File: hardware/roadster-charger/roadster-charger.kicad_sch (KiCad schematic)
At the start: 62 parts, among them J1 USB4505-03-0-A, J2 USB4505-03-0-A, J3 54-00166, Q1 CSD19532Q5B, U1 FUSB307BMPX, U10 OPA340NA, U11 LM75B, U2 ESP32-C3-MINI-1, U3 INA168, U4 LM5050-1, U5 INA168, U6 OPA340NA, U9 MPM3606AGQV-P

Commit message: add in some missing PNs
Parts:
- H1, H2: MPN (none) -> DNP; now left out of the parts list
- TP1, TP2, TP3, TP4: MPN (none) -> RCU-0C
- U11: MPN (none) -> LM75BDP
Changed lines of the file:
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@@
 (kicad_sch (version 20230121) (generator eeschema)
   (paper "B")
+  (title_block
+    (rev "1")
+  )
   (junction (at 133.35 78.74) (diameter 0) (color 0 0 0 0)
   )
@@
   )
   (symbol (lib_id "Mechanical:MountingHole") (at 400.05 238.76 0) (unit 1)
-    (in_bom yes) (on_board yes) (dnp no) (fields_autoplaced)
+    (in_bom no) (on_board yes) (dnp no) (fields_autoplaced)
     (property "Reference" "H1" (at 402.59 237.49 0)
       (effects (font (size 1.27 1.27)) (justify left))
@@
       (effects (font (size 1.27 1.27)) hide)
     )
+    (property "MPN" "DNP" (at 400.05 238.76 0)
+      (effects (font (size 1.27 1.27)) hide)
+    )
     (instances
       (project "roadster-charger"
@@
   )
   (symbol (lib_id "Mechanical:MountingHole") (at 400.05 245.11 0) (unit 1)
-    (in_bom yes) (on_board yes) (dnp no) (fields_autoplaced)
+    (in_bom no) (on_board yes) (dnp no) (fields_autoplaced)
     (property "Reference" "H2" (at 402.59 243.84 0)
       (effects (font (size 1.27 1.27)) (justify left))
@@
       (effects (font (size 1.27 1.27)) hide)
     )
+    (property "MPN" "DNP" (at 400.05 245.11 0)
+      (effects (font (size 1.27 1.27)) hide)
+    )
     (instances
       (project "roadster-charger"
@@
       (effects (font (size 1.27 1.27)) hide)
     )
+    (property "MPN" "LM75BDP" (at 189.23 180.34 0)
+      (effects (font (size 1.27 1.27)) hide)
+    )
     (pin "6")
     (pin "8")
@@
       (effects (font (size 1.27 1.27)) hide)
     )
+    (property "MPN" "RCU-0C" (at 201.93 31.75 0)
+      (effects (font (size 1.27 1.27)) hide)
+    )
     (pin "1")
     (instances
@@
       (effects (font (size 1.27 1.27)) hide)
     )
+    (property "MPN" "RCU-0C" (at 119.38 219.71 0)
+      (effects (font (size 1.27 1.27)) hide)
+    )
     (pin "1")
     (instances
@@
       (effects (font (size 1.27 1.27)) hide)
     )
+    (property "MPN" "RCU-0C" (at 191.77 31.75 0)
+      (effects (font (size 1.27 1.27)) hide)
+    )
     (pin "1")
     (instances
@@
       (effects (font (size 1.27 1.27)) hide)
     )
+    (property "MPN" "RCU-0C" (at 196.85 31.75 0)
+      (effects (font (size 1.27 1.27)) hide)
+    )

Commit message: run schematic annotation to clean up error
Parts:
- removed H1, H2: MountingHole, MountingHole:MountingHole_3.2mm_M3_ISO7380_Pad_TopBottom, symbol Mechanical:MountingHole
- added H1, H2: MountingHole_Pad, MountingHole:MountingHole_3.2mm_M3_ISO7380_Pad_TopBottom, symbol Mechanical:MountingHole_Pad
- renumbered C4 to C10, C5 to C11, C22 to C12, C8 to C13, C9 to C14, C21 to C15, C6 to C16, C10 to C3, C3 to C4, C18 to C5, C11 to C6, C20 to C7, C27 to C8, C19 to C9, D5 to D4, D4 to D5, D7 to D6, R5 to R1, R2 to R10, R3 to R11, R4 to R12, R9 to R13, R12 to R14, R13 to R15, R8 to R16, R6 to R17, R10 to R18, R11 to R19, R19 to R2, R23 to R20, R24 to R21, R21 to R3, R26 to R4, R20 to R5, R25 to R6, R22 to R7, R7 to R8, R1 to R9, TP4 to TP1, TP1 to TP2, TP2 to TP3, TP3 to TP4, U9 to U1, U10 to U4, U1 to U5, U11 to U6, U4 to U7, U5 to U8, U6 to U9
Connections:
- net GND: now also H1.1, H2.1

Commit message: clean up fab layer, add value to test points
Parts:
- TP1, TP2, TP3, TP4: value TestPoint -> RCU-0C
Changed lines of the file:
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@@
       (effects (font (size 1.27 1.27)) (justify left))
     )
-    (property "Value" "TestPoint" (at 204.47 29.718 0)
+    (property "Value" "RCU-0C" (at 204.47 29.718 0)
       (effects (font (size 1.27 1.27)) (justify left) hide)
     )
@@
       (effects (font (size 1.27 1.27)) (justify left))
     )
-    (property "Value" "TestPoint" (at 116.84 221.742 0)
+    (property "Value" "RCU-0C" (at 116.84 221.742 0)
       (effects (font (size 1.27 1.27)) (justify left) hide)
     )
@@
       (effects (font (size 1.27 1.27)) (justify left))
     )
-    (property "Value" "TestPoint" (at 194.31 29.718 0)
+    (property "Value" "RCU-0C" (at 194.31 29.718 0)
       (effects (font (size 1.27 1.27)) (justify left) hide)
     )
@@
       (effects (font (size 1.27 1.27)) (justify left))
     )
-    (property "Value" "TestPoint" (at 199.39 29.718 0)
+    (property "Value" "RCU-0C" (at 199.39 29.718 0)
       (effects (font (size 1.27 1.27)) (justify left) hide)
     )

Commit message: add IO9 test point for when I accidentally reassign usb pins during fw dev
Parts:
- added TP1: RCU-0C, RCU-0C:TP+195X110, symbol Connector:TestPoint
- renumbered TP1 to TP2, TP2 to TP3, TP3 to TP4, TP4 to TP5
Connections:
- net IO9_BOOT: now reaches U2.23 (GPIO9)
- net IO9_BOOT: now also TP1.1
- no-connect marks 25 -> 24
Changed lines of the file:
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@@
   (no_connect (at 58.42 57.15))
   (no_connect (at 179.07 182.88))
-  (no_connect (at 96.52 234.95))
   (no_connect (at 179.07 43.18))
   (no_connect (at 179.07 53.34))
@@
     (stroke (width 0) (type default))
   )
+  (wire (pts (xy 96.52 234.95) (xy 111.76 234.95))
+    (stroke (width 0) (type default))
+  )
   (wire (pts (xy 287.02 161.29) (xy 292.1 161.29))
     (stroke (width 0) (type default))
@@
     (effects (font (size 1.27 1.27)) (justify right bottom))
   )
+  (label "IO9_BOOT" (at 109.22 234.95 180) (fields_autoplaced)
+    (effects (font (size 1.27 1.27)) (justify right bottom))
+  )
   (label "V_SW" (at 71.12 138.43 0) (fields_autoplaced)
     (effects (font (size 1.27 1.27)) (justify left bottom))
@@
     )
   )
+  (symbol (lib_id "Connector:TestPoint") (at 111.76 234.95 270) (unit 1)
+    (in_bom yes) (on_board yes) (dnp no)
+    (property "Reference" "TP1" (at 113.03 232.41 90)
+      (effects (font (size 1.27 1.27)) (justify left))
+    )
+    (property "Value" "RCU-0C" (at 113.792 237.49 0)
+      (effects (font (size 1.27 1.27)) (justify left) hide)
+    )
+    (property "Footprint" "RCU-0C:TP+195X110" (at 111.76 240.03 0)
+      (effects (font (size 1.27 1.27)) hide)
+    )
+    (property "Datasheet" "~" (at 111.76 240.03 0)
+      (effects (font (size 1.27 1.27)) hide)
+    )
+    (property "MPN" "RCU-0C" (at 111.76 234.95 0)
+      (effects (font (size 1.27 1.27)) hide)
+    )
+    (pin "1")
+    (instances
+      (project "roadster-charger"
+        (path "/57ecac41-cd8a-4182-a81e-fed3e381aedd"
+          (reference "TP1") (unit 1)
+        )
+      )
+    )
+  )
   (symbol (lib_id "Device:R_Small") (at 222.25 29.21 0) (unit 1)
     (in_bom yes) (on_board yes) (dnp no)
@@
   (symbol (lib_id "Connector:TestPoint") (at 201.93 31.75 0) (unit 1)
     (in_bom yes) (on_board yes) (dnp no)
-    (property "Reference" "TP4" (at 200.025 26.035 0)
+    (property "Reference" "TP5" (at 200.025 26.035 0)
       (effects (font (size 1.27 1.27)) (justify left))
     )
@@
       (project "roadster-charger"
         (path "/57ecac41-cd8a-4182-a81e-fed3e381aedd"
-          (reference "TP4") (unit 1)
+          (reference "TP5") (unit 1)
         )
       )
@@
   (symbol (lib_id "Connector:TestPoint") (at 119.38 219.71 180) (unit 1)
     (in_bom yes) (on_board yes) (dnp no)
-    (property "Reference" "TP1" (at 121.285 225.425 0)
+    (property "Reference" "TP2" (at 121.285 225.425 0)
       (effects (font (size 1.27 1.27)) (justify left))
     )
@@
       (project "roadster-charger"
         (path "/57ecac41-cd8a-4182-a81e-fed3e381aedd"
-          (reference "TP1") (unit 1)
+          (reference "TP2") (unit 1)
         )
       )
@@
   (symbol (lib_id "Connector:TestPoint") (at 191.77 31.75 0) (unit 1)
     (in_bom yes) (on_board yes) (dnp no)
-    (property "Reference" "TP2" (at 189.865 26.035 0)
+    (property "Reference" "TP3" (at 189.865 26.035 0)
       (effects (font (size 1.27 1.27)) (justify left))
     )
@@
       (project "roadster-charger"
         (path "/57ecac41-cd8a-4182-a81e-fed3e381aedd"
-          (reference "TP2") (unit 1)
+          (reference "TP3") (unit 1)
         )
       )
@@
   (symbol (lib_id "Connector:TestPoint") (at 196.85 31.75 0) (unit 1)
     (in_bom yes) (on_board yes) (dnp no)
-    (property "Reference" "TP3" (at 194.945 26.035 0)
+    (property "Reference" "TP4" (at 194.945 26.035 0)
       (effects (font (size 1.27 1.27)) (justify left))
     )
@@
       (project "roadster-charger"
         (path "/57ecac41-cd8a-4182-a81e-fed3e381aedd"
-          (reference "TP3") (unit 1)
+          (reference "TP4") (unit 1)
         )
       )

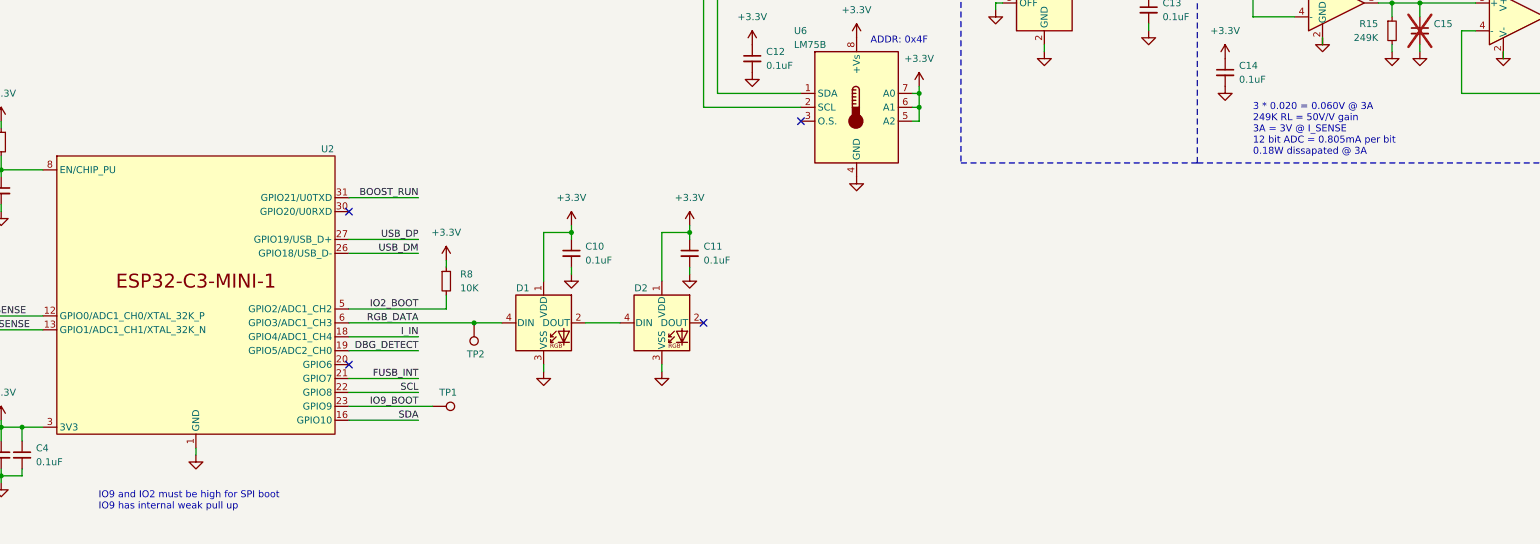
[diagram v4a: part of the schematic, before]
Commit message: correct schem comments for 2.5V max ADC input
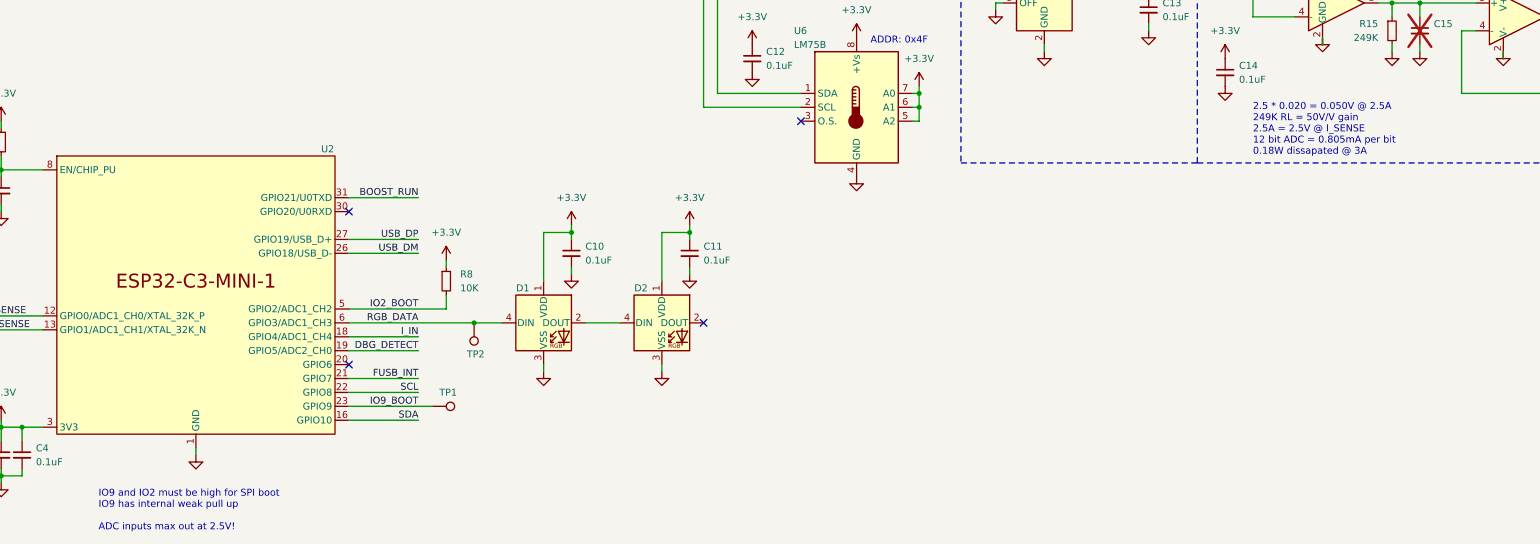
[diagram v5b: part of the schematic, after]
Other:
- note added: "2.5 * 0.020 = 0.050V @ 2.5A 249K RL = 50V/V gain 2.5A = 2.5V @ I_SENSE 12 bit ADC = 0.805mA per bit 0.18W dissapated @ 3A"
- note added: "IO9 and IO2 must be high for SPI boot IO9 has internal weak pull up ADC inputs max out at 2.5V!"
- note removed: "3 * 0.020 = 0.060V @ 3A 249K RL = 50V/V gain 3A = 3V @ I_SENSE 12 bit ADC = 0.805mA per bit 0.18W dissapated @ 3A"
- note removed: "IO9 and IO2 must be high for SPI boot IO9 has internal weak pull up"
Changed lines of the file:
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@@
     (effects (font (size 1.27 1.27)) (justify left bottom))
   )
-  (text "IO9 and IO2 must be high for SPI boot\nIO9 has internal weak pull up"
-    (at 50.8 254 0)
+  (text "IO9 and IO2 must be high for SPI boot\nIO9 has internal weak pull up\n\nADC inputs max out at 2.5V!"
+    (at 50.8 257.81 0)
     (effects (font (size 1.27 1.27)) (justify left bottom))
   )
@@
     (effects (font (size 1.27 1.27)) (justify left bottom))
   )
-  (text "3 * 0.020 = 0.060V @ 3A\n249K RL = 50V/V gain\n3A = 3V @ I_SENSE\n12 bit ADC = 0.805mA per bit\n0.18W dissapated @ 3A"
+  (text "2.5 * 0.020 = 0.050V @ 2.5A\n249K RL = 50V/V gain\n2.5A = 2.5V @ I_SENSE\n12 bit ADC = 0.805mA per bit\n0.18W dissapated @ 3A"
     (at 261.62 189.23 0)
     (effects (font (size 1.27 1.27)) (justify left bottom))

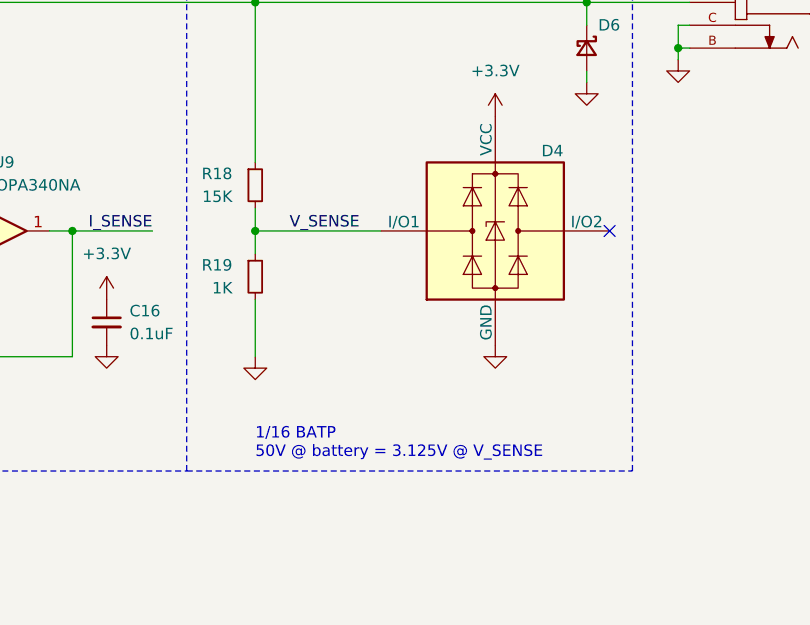
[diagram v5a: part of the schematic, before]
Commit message: change vout voltage divider to target max 2.5V @ 50V at battery
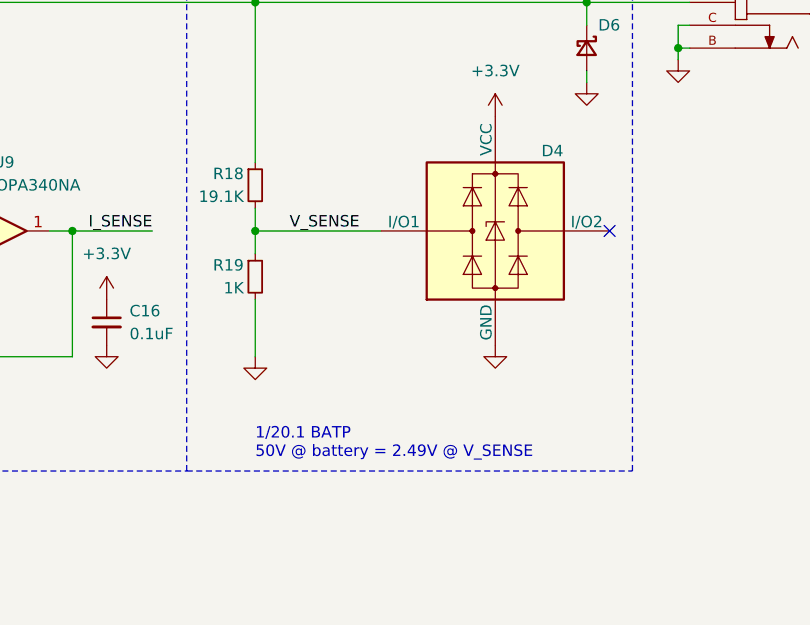
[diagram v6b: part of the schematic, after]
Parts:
- R18: value 15K -> 19.1K; MPN RC0603JR-0715KL -> RMCF0603FT19K1
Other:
- note added: "1/20.1 BATP 50V @ battery = 2.49V @ V_SENSE"
- note removed: "1/16 BATP 50V @ battery = 3.125V @ V_SENSE"
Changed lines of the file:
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@@
     (effects (font (size 1.27 1.27)) (justify left bottom))
   )
-  (text "1/16 BATP\n50V @ battery = 3.125V @ V_SENSE" (at 340.36 189.23 0)
+  (text "1/20.1 BATP\n50V @ battery = 2.49V @ V_SENSE" (at 340.36 189.23 0)
     (effects (font (size 1.27 1.27)) (justify left bottom))
   )
@@
   (symbol (lib_id "Device:R_Small") (at 340.36 158.75 0) (unit 1)
     (in_bom yes) (on_board yes) (dnp no)
-    (property "Reference" "R18" (at 337.82 157.48 0)
-      (effects (font (size 1.27 1.27)) (justify right))
-    )
-    (property "Value" "15K" (at 337.82 160.02 0)
+    (property "Reference" "R18" (at 339.09 157.48 0)
+      (effects (font (size 1.27 1.27)) (justify right))
+    )
+    (property "Value" "19.1K" (at 339.09 160.02 0)
       (effects (font (size 1.27 1.27)) (justify right))
     )
@@
       (effects (font (size 1.27 1.27)) hide)
     )
-    (property "MPN" "RC0603JR-0715KL" (at 340.36 158.75 0)
+    (property "MPN" "RMCF0603FT19K1" (at 340.36 158.75 0)
       (effects (font (size 1.27 1.27)) hide)
     )
@@
   (symbol (lib_id "Device:R_Small") (at 340.36 168.91 0) (unit 1)
     (in_bom yes) (on_board yes) (dnp no)
-    (property "Reference" "R19" (at 337.82 167.64 0)
-      (effects (font (size 1.27 1.27)) (justify right))
-    )
-    (property "Value" "1K" (at 337.82 170.18 0)
-      (effects (font (size 1.27 1.27)) (justify right))
-    )
+    (property "Reference" "R19" (at 339.09 167.64 0)
+      (effects (font (size 1.27 1.27)) (justify right))
+    )
+    (property "Value" "1K" (at 339.09 170.18 0)
+      (effects (font (size 1.27 1.27)) (justify right))
+    )

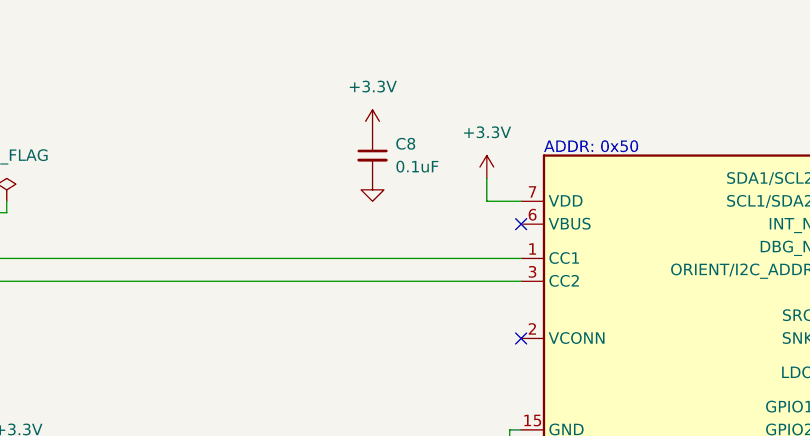
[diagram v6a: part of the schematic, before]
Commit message: connect FUSB307 vbus pin
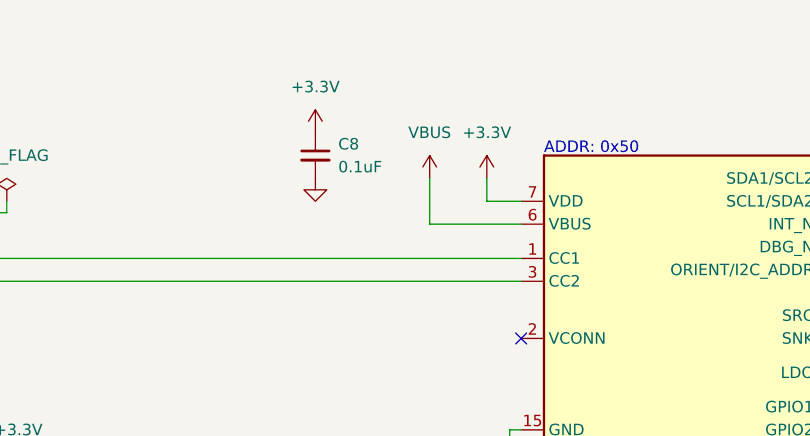
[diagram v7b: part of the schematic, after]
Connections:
- net VBUS: now also U5.6 (VBUS)
- no-connect marks 24 -> 23
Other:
- moved on the sheet: C8

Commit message: Update to KiCad 8 + sneaky resistor PN correction
Update checkout and artifact actions
Remove specific board outputs from actions file (kicad bug fixed now)
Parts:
- R14: MPN LVT06R0020HER -> ERJ-3BWFR020V
